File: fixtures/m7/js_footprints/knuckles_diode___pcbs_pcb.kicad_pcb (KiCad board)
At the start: 2 copper layers, 1 part

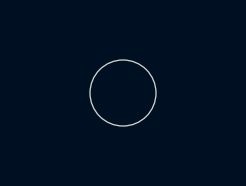
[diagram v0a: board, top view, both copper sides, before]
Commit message: feat: add js footprint parity and fixtures
- Implement native JS footprints behind "js-footprints" feature via Boa\n- Switch reference outputs to classic JSCAD v1 for upstream/GUI parity\n- Fix KiCad Edge.Cuts winding/order differences vs upstream\n- Improve YAML normalization (expressions/holes/trailing commas) for upstream config compatibility\n- Add M7 fixtures + goldens for js footprints
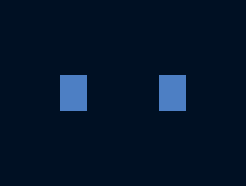
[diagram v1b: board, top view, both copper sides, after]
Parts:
- removed MH1: , ceoloide:mounting_hole_npth
- added D1: , ceoloide:diode_tht_sod123, B.Cu at (0.00, 0.00)
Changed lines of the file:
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@@
   )
   (net 0 "")
-  (footprint "ceoloide:mounting_hole_npth"
-    (layer "F.Cu")
-    (at 0 0 0)
-    (property "Reference" "MH1"
-      (at 0 2.55 0)
-      (layer "F.SilkS")
-      hide
-      (effects (font (size 1 1) (thickness 0.15)))
-    )
-    (pad "" np_thru_hole circle
-      (at 0 0 0)
-      (size 2.2 2.2)
-      (drill 2.2)
-      (layers "*.Cu" "*.Mask")
-    )
-  )
+(net 1 "GND")
+(net 2 "ROW1")
+    (footprint "ceoloide:diode_tht_sod123"
+        (layer "B.Cu")
+        (at 0 0 0)
+        (property "Reference" "D1"
+            (at 0 0 0)
+            (layer "B.SilkS")
+            hide
+            (effects (font (size 1 1) (thickness 0.15)))
+        )
+        (fp_line (start 0.25 0) (end 0.75 0) (layer "B.SilkS") (stroke (width 0.1) (type solid)))
+        (fp_line (start 0.25 0.4) (end -0.35 0) (layer "B.SilkS") (stroke (width 0.1) (type solid)))
+        (fp_line (start 0.25 -0.4) (end 0.25 0.4) (layer "B.SilkS") (stroke (width 0.1) (type solid)))
+        (fp_line (start -0.35 0) (end 0.25 -0.4) (layer "B.SilkS") (stroke (width 0.1) (type solid)))
+        (fp_line (start -0.35 0) (end -0.35 0.55) (layer "B.SilkS") (stroke (width 0.1) (type solid)))
+        (fp_line (start -0.35 0) (end -0.35 -0.55) (layer "B.SilkS") (stroke (width 0.1) (type solid)))
+        (fp_line (start -0.75 0) (end -0.35 0) (layer "B.SilkS") (stroke (width 0.1) (type solid)))
+        (pad "2" smd rect (at 1.65 0 0) (size 0.9 1.2) (layers "B.Cu" "B.Paste" "B.Mask") (net 1 "GND"))
+        (pad "1" smd rect (at -1.65 0 0) (size 0.9 1.2) (layers "B.Cu" "B.Paste" "B.Mask") (net 2 "ROW1"))
+        )
 )
